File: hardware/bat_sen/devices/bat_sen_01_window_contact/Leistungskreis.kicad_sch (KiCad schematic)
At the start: 2 parts, among them SW1 SW_Reed

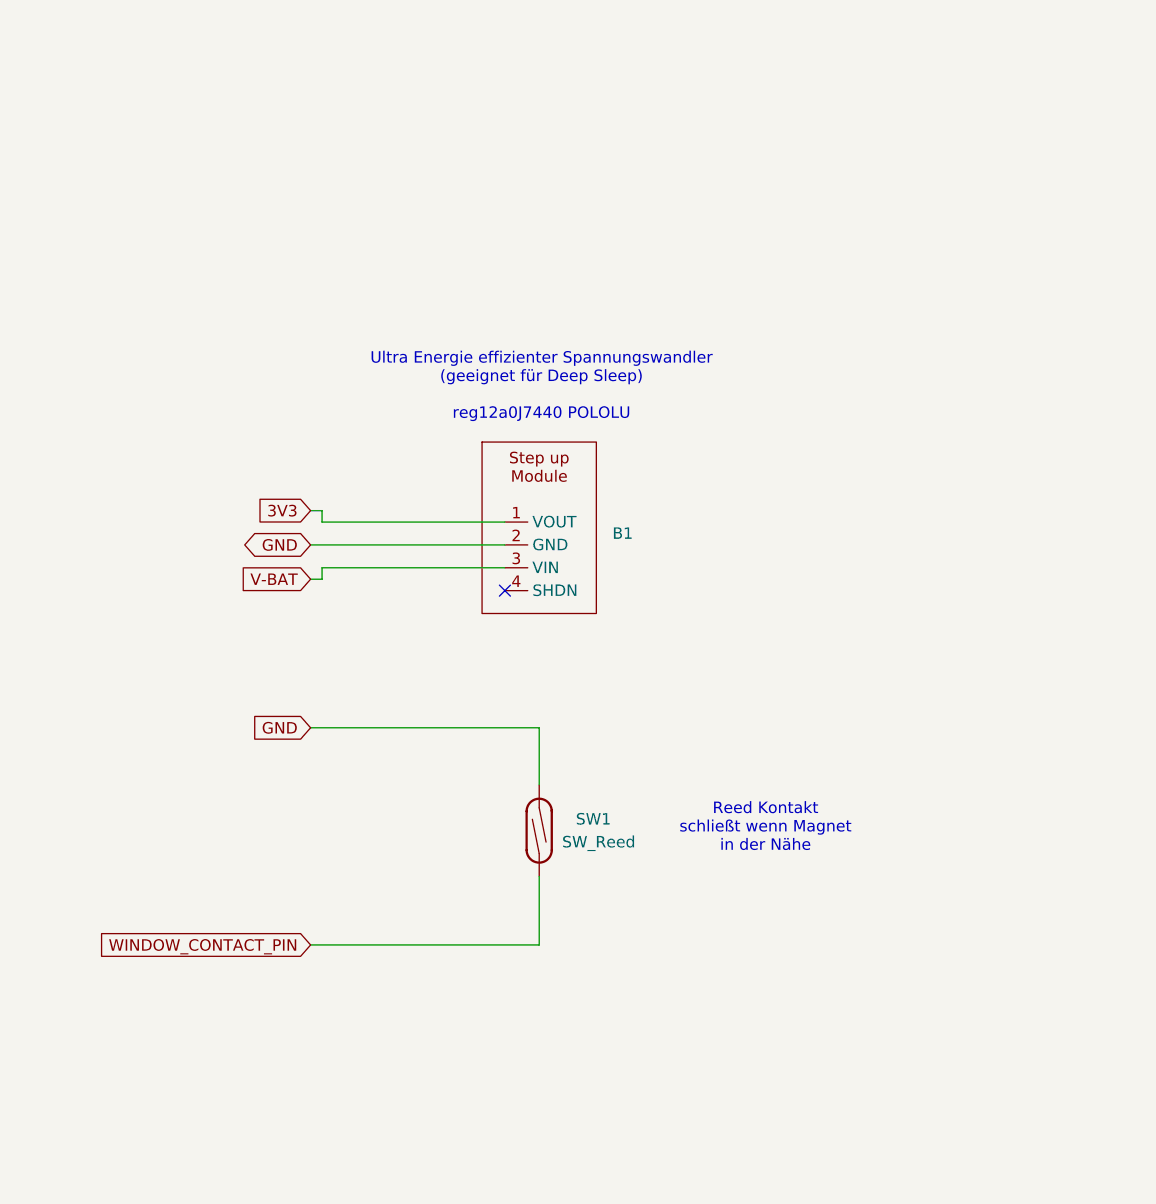
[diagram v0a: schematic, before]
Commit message: öffentliche Präsentation bereinigt: KI-Referenzen entfernt, READMEs optimiert, Firmware als Hauptlinie, ESPHome als Alternative mit Disclaimer
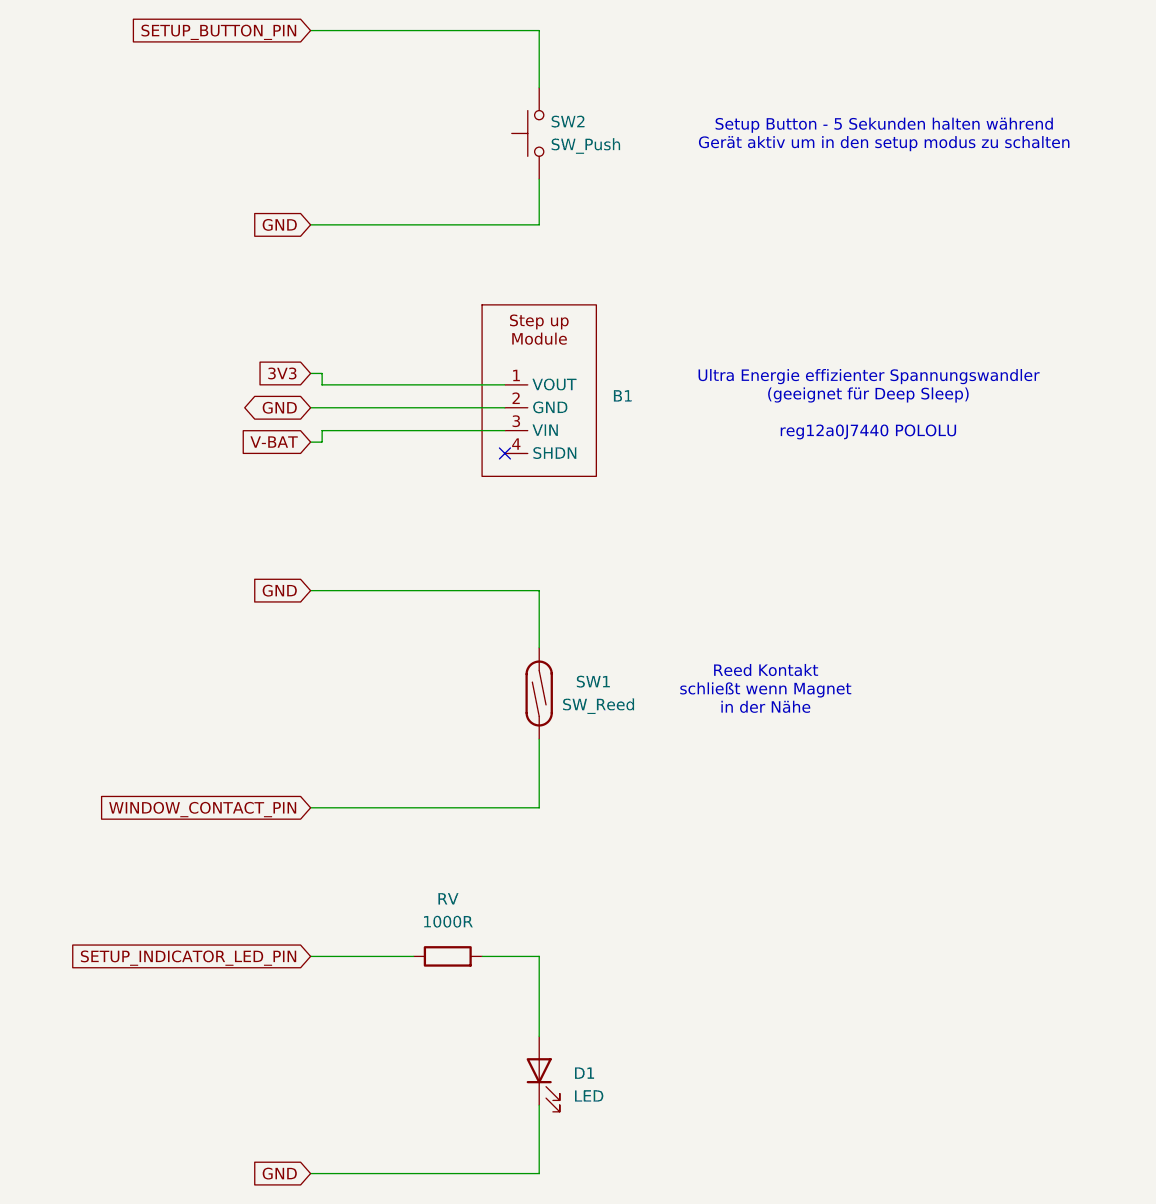
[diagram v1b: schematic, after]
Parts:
- added D1: LED, symbol Device:LED
- added RV: 1000R, symbol Device:R
- added SW2: SW_Push, symbol Switch:SW_Push
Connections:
- net GND: now also D1.1 (K), SW2.1
- new net: D1.2 (A), RV.2
- new net SETUP_BUTTON_PIN: SW2.2
- new net SETUP_INDICATOR_LED_PIN: RV.1
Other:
- note added: "Setup Button - 5 Sekunden halten während Gerät aktiv um in den setup modus zu schalten"
- moved on the sheet: B1, SW1
